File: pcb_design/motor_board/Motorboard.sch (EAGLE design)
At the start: 74 parts, among them M1 STEPPER_MOTOR_SMD, M2 STEPPER_MOTOR_SMD

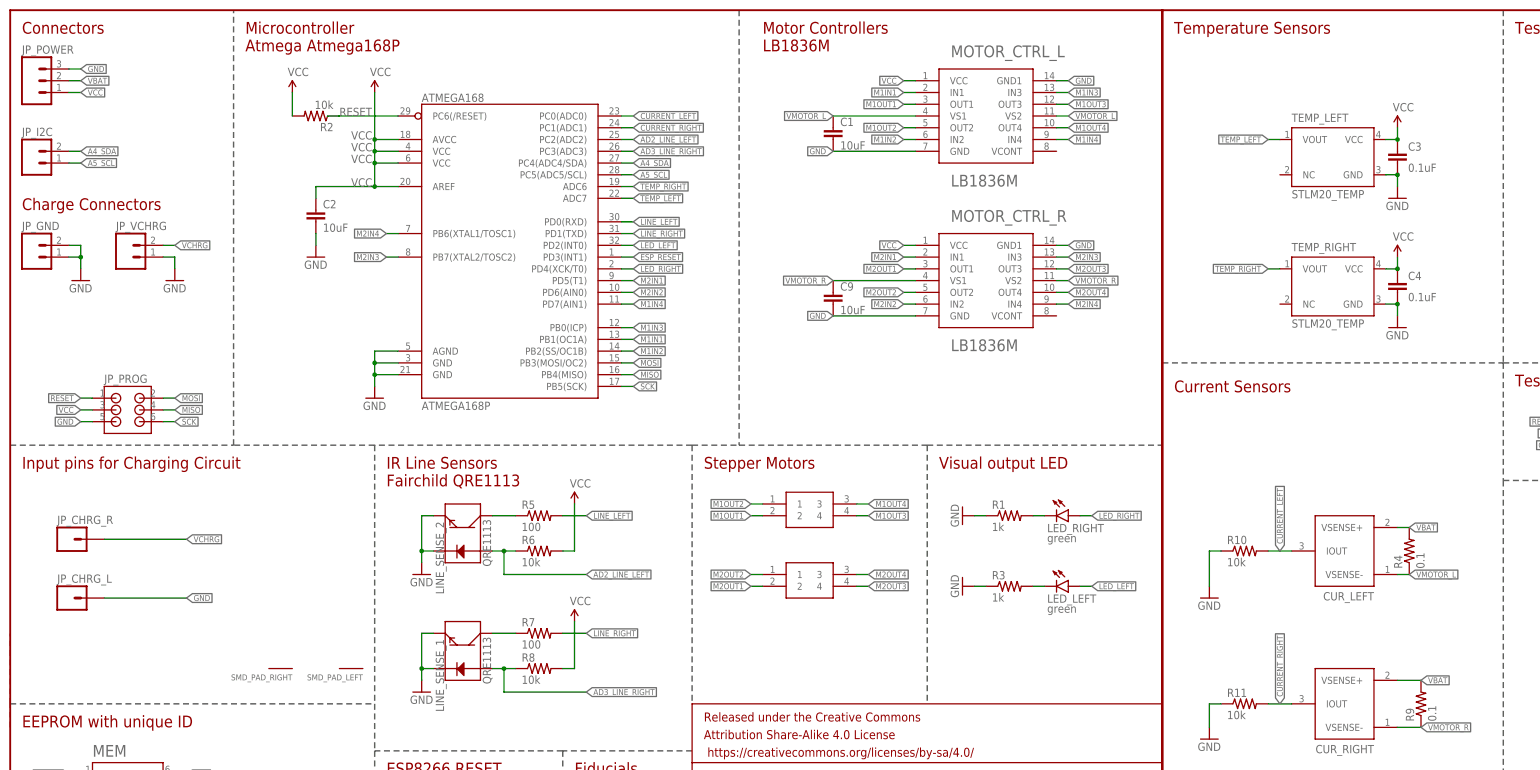
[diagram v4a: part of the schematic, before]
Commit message: Minor silk screen changes to mMotor board
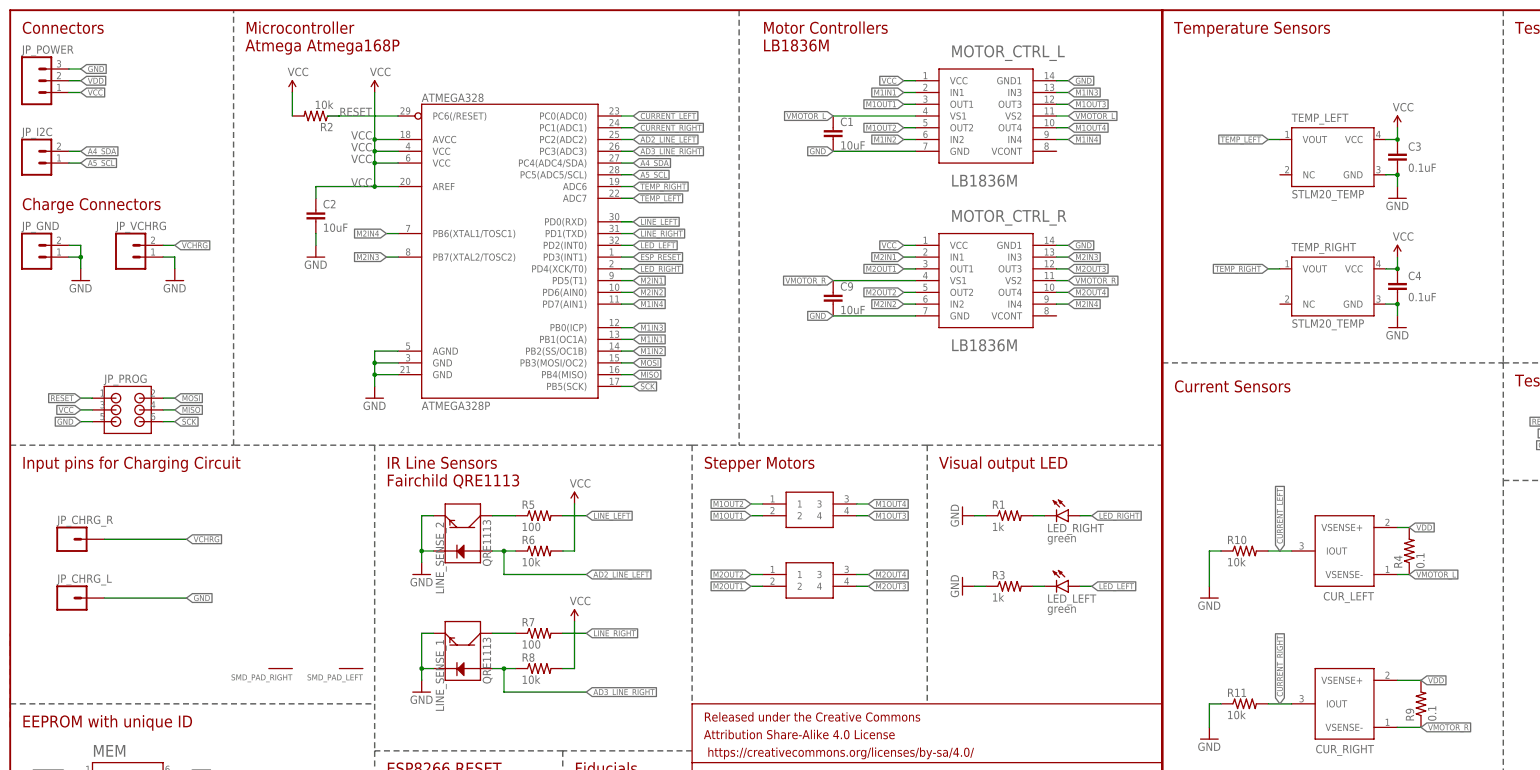
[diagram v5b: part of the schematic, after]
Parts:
- ATMEGA328P: value ATMEGA168 -> ATMEGA328
- JP_CHRG_L, JP_CHRG_R: value M01NOSILK-KIT -> (none)
- renumbered ATMEGA168P to ATMEGA328P
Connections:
- net VBAT renamed VDD

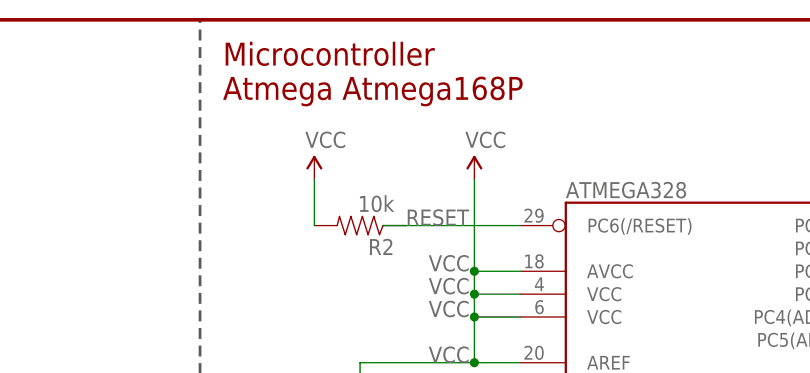
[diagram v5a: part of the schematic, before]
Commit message: Minor comment change on motor board schematic
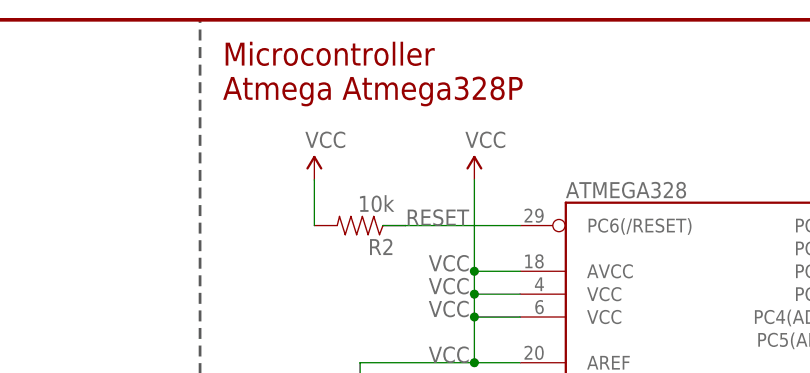
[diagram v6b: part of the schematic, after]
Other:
- note added: "Microcontroller Atmega Atmega328P"
- note removed: "Microcontroller Atmega Atmega168P"
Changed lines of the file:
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@@
 <text x="2.54" y="180.34" size="2.54" layer="94">Connectors</text>
 <text x="50.8" y="176.53" size="2.54" layer="94">Microcontroller
-Atmega Atmega168P</text>
+Atmega Atmega328P</text>
 <wire x1="147.32" y1="91.44" x2="78.74" y2="91.44" width="0.3048" layer="97" style="shortdash"/>
 <wire x1="78.74" y1="91.44" x2="48.26" y2="91.44" width="0.3048" layer="97" style="shortdash"/>
